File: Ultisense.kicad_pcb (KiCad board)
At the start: 2 copper layers, 44.7 x 93.6 mm, 94 parts, among them J1 USB_C_Receptacle_USB2.0_14P, J2 Conn_01x02, J3 Micro_SD_Card, J5 Conn_02x08_Odd_Even, J6 Conn_02x02_Odd_Even, J7 Conn_02x08_Top_Bottom, SW2 SW_Push, SW3 SW_Push, U1 ESP32-S3-WROOM-1, U10 ST25DV04KC-IE6S3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

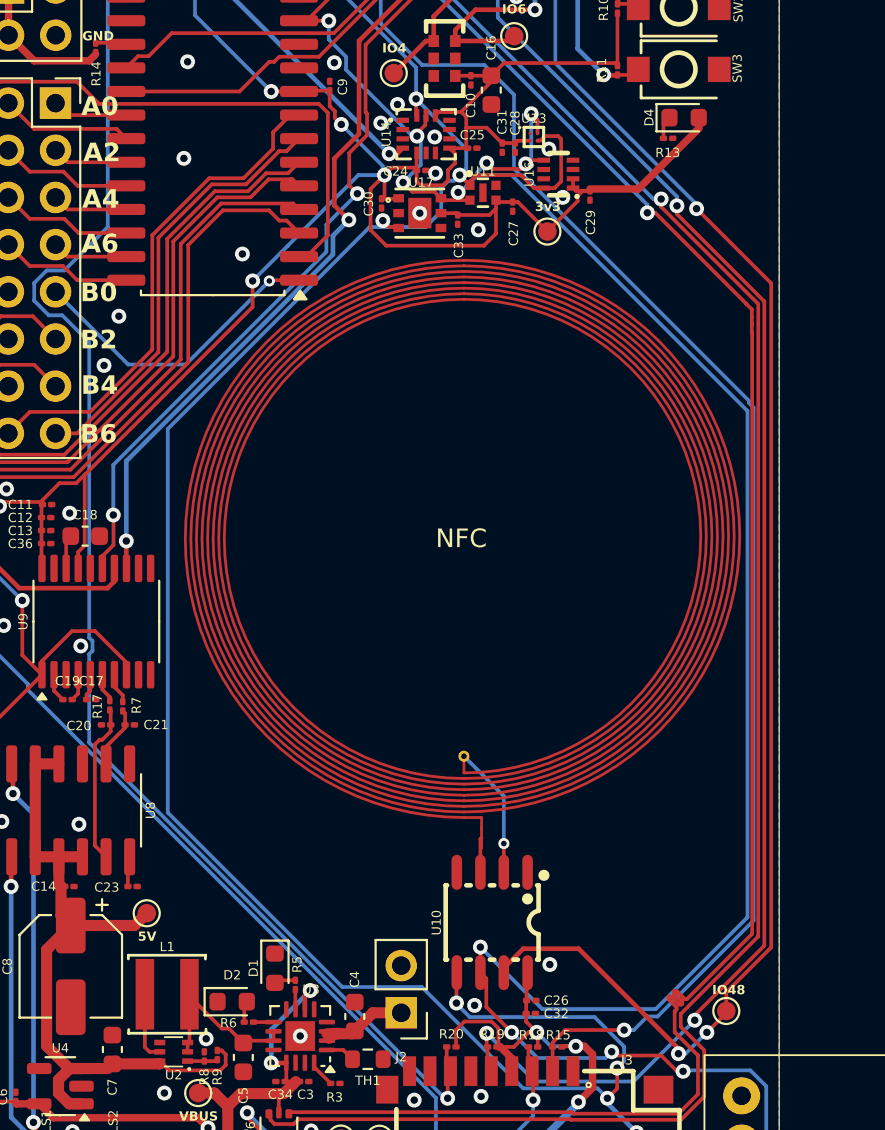
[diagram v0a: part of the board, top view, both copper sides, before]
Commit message: replaced out of stock light sensor
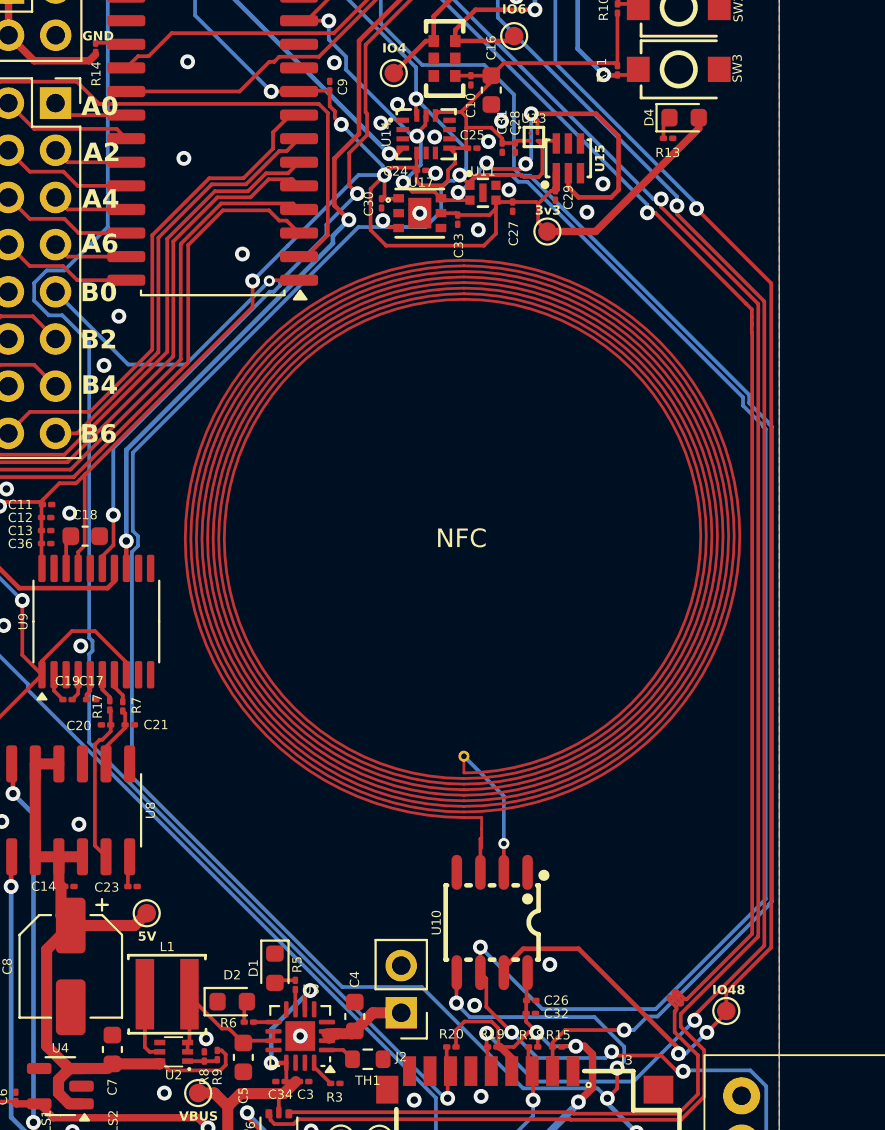
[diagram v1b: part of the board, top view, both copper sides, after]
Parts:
- removed U16: OPT4048DTSR, easyeda2kicad:SOT-5X3-8_L2.1-W1.2-P0.50-LS1.9-BL
- added U15: TCS34001FNM, easyeda2kicad:DFN-6_L2.4-W2.0-P0.65-BL, F.Cu at (160.2, 78.4)
- moved C29 1.86 mm to (159.5, 80.4)
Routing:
- net SCL: track 144.6 -> 156.9 mm
- net +3V3: track 303.6 -> 304.8 mm
- net IO10: track 80.0 -> 81.0 mm
- net GND: vias 61 -> 64

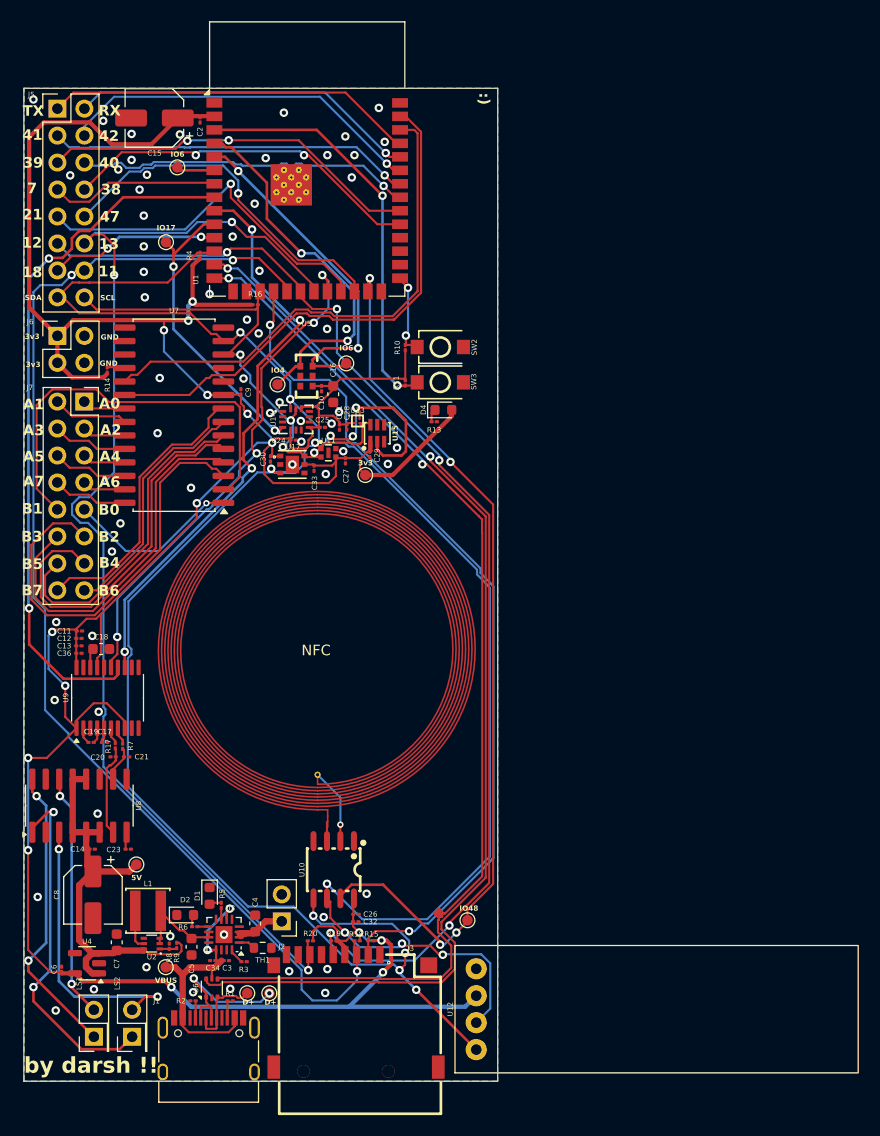
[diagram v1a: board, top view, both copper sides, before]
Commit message: replaced 01005 with 0201, fixed a few other things, reordering
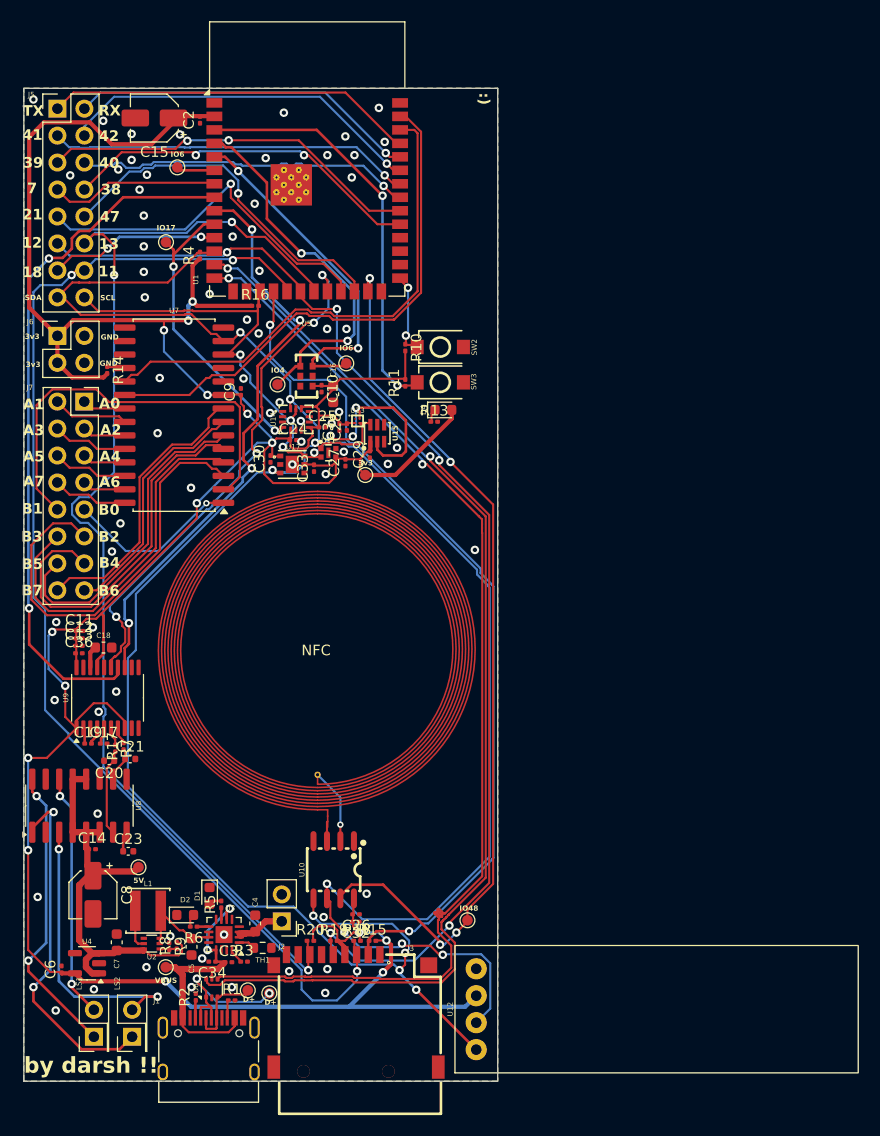
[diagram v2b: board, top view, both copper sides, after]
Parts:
- C10, C2, C24, C25, C26, C27, C28, C29, C30, C34, C36, C9: value 0.1uF -> 1uF; footprint Capacitor_SMD:C_01005_0402Metric -> Capacitor_SMD:C_0201_0603Metric
- C11, C12, C13, C14, C17, C19, C3, C31, C32, C33, C6: value 1uF -> 4.7uF; footprint Capacitor_SMD:C_01005_0402Metric -> Capacitor_SMD:C_0201_0603Metric
- C15, C8: footprint Capacitor_SMD:CP_Elec_5x5.3 -> Capacitor_SMD:CP_Elec_4x5.4
- C20, C21, C23: footprint Capacitor_SMD:C_01005_0402Metric -> Capacitor_SMD:C_0402_1005Metric
- R1, R10, R11, R13, R14, R15, R16, R17, R18, R19, R2, R20, R3, R4, R5, R6, R7, R8, R9: footprint Resistor_SMD:R_01005_0402Metric -> Resistor_SMD:R_0201_0603Metric
- moved C20 0.53 mm to (134.9, 109.3)
- moved R2 0.44 mm to (143.1, 131.5), turned to 90 degrees
- moved C21 0.39 mm to (136.9, 109.1)
- moved 5V 0.33 mm to (137.7, 119.3)
- moved C19 0.31 mm to (132.9, 107.7)
- moved D+ 0.27 mm to (148.0, 130.9)
- moved C18 0.26 mm to (134.4, 98.6)
- moved C3 0.25 mm to (146.2, 128.2)
- moved R7 0.25 mm to (135.5, 108.1)
- moved C23 0.20 mm to (136.7, 117.8)
- moved C27 0.18 mm to (157.2, 81.2)
- moved R15 0.15 mm to (159.8, 126.2)
- moved R1 0.15 mm to (146.5, 131.8)
- moved C17 0.14 mm to (134.4, 107.7)
- moved C34 0.11 mm to (144.6, 128.2)
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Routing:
- net IO14: track 48.4 -> 49.6 mm
- net +3V3: track 304.8 -> 305.6 mm
- net VBUS: track 26.8 -> 27.3 mm
- net GND: vias 64 -> 67
